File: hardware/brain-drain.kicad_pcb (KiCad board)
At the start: 4 copper layers, 136 x 100 mm, 301 parts, among them J10 SATA 22-pin, J11 SATA 22-pin, J12 SATA 22-pin, J13 SATA 22-pin, J21 KPJX-4S-S, J3 microSD, J40 Fan GND/5V/TACH/PWM, J41 OLED GND/VCC/SCL/SDA, J5 USB-C rpiboot, J50 M.2 M-key, J6 nRPIBOOT, J7 UART0 GND/TX/RX, M1 CM5002016, Q20 AO4407A, Q31 P-FET -30V 6A DFN3x3, Q32 P-FET -30V 6A DFN3x3, Q33 P-FET -30V 6A DFN3x3, Q34 P-FET -30V 6A DFN3x3, Q41 P-FET -30V 6A DFN3x3, Q42 P-FET -30V 6A DFN3x3, Q43 P-FET -30V 6A DFN3x3, Q44 P-FET -30V 6A DFN3x3, Q51 2N7002, Q52 2N7002, Q53 2N7002, Q54 2N7002, Q61 2N7002, Q62 2N7002, Q63 2N7002, Q64 2N7002, SW1 DIP x8, SW3 lid microswitch, U1 USB5744/2G, U10 ASM1153E, U11 ASM1153E, U12 ASM1153E, U13 ASM1153E, U2 USB5744/2G, U20 TPS56637RPAR, U21 TPS56637RPAR, U22 AP63203WU-7, U3 AP2112K-1.2, U50 TPS22965DSGR, U51 AP63203WU-7, U52 TPS22965DSGR, Y1 25MHz CL=20pF, Y10 30MHz CL=16pF, Y11 30MHz CL=16pF, Y12 30MHz CL=16pF, Y13 30MHz CL=16pF, Y2 25MHz CL=20pF

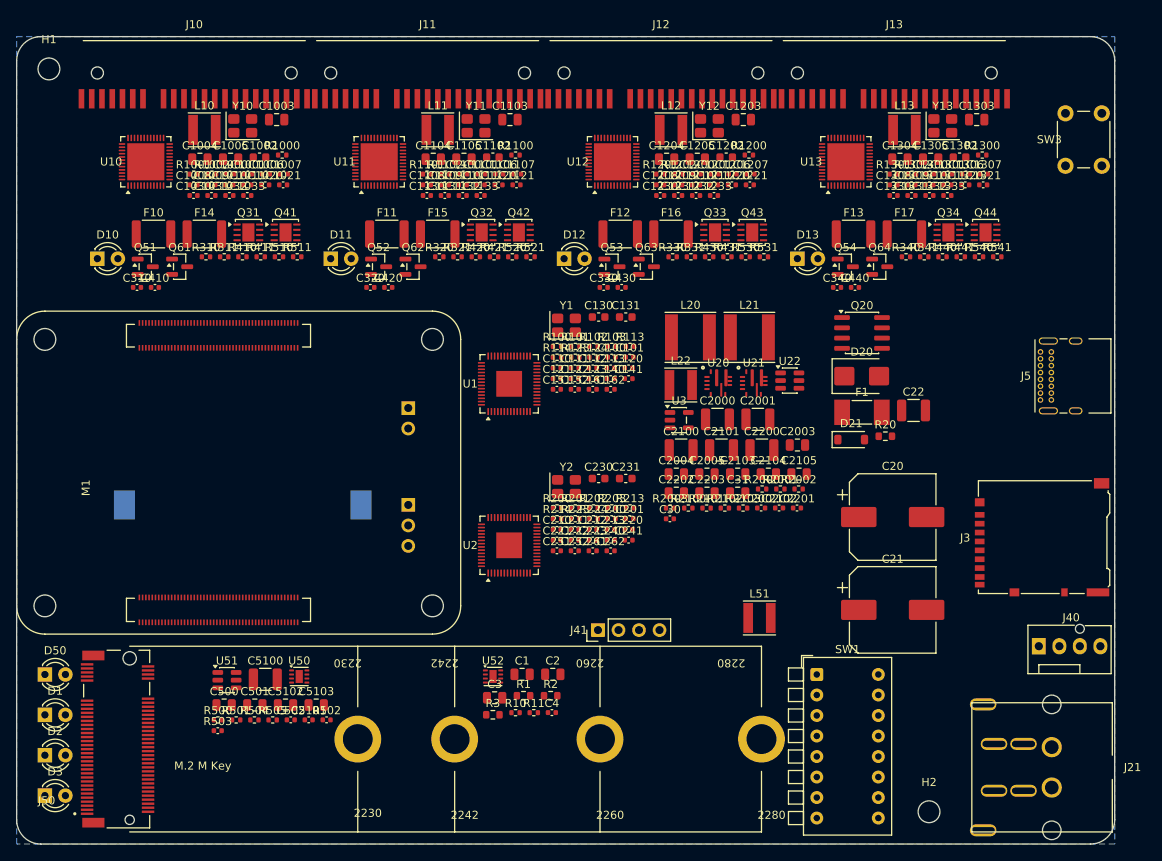
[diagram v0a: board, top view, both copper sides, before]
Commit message: hw(routing): v2 board autorouted — 75/75 signal nets, fanout and net-class fixes
- route.py: net classes written to brain-drain.kicad_pro (gen_sch.py preserves them); prepare keeps
  existing zones (deleting filled zones with fanout vias corrupts the pcbnew bindings); fanout checks
  the plane polygon instead of its bbox; import strips keep-out crossings; run_freerouting uses the
  lite DSN with -oit 2
- routed board: 930 segments / 4.4 m, 214 vias; DRC 1 known starved-thermal note, 0 clearance errors;
  499 open connections are planes, rails, bays and pairs for the hand pass
- render_board.sh: board PNGs cropped to the outline, schematic PDF + sheet PNGs
- docs: STATUS R16 closed, R4 detailed, USAGE pitfalls, CHANGELOG, tracker

Co-Authored-By: Claude Fable 5.1 <noreply@anthropic.com>
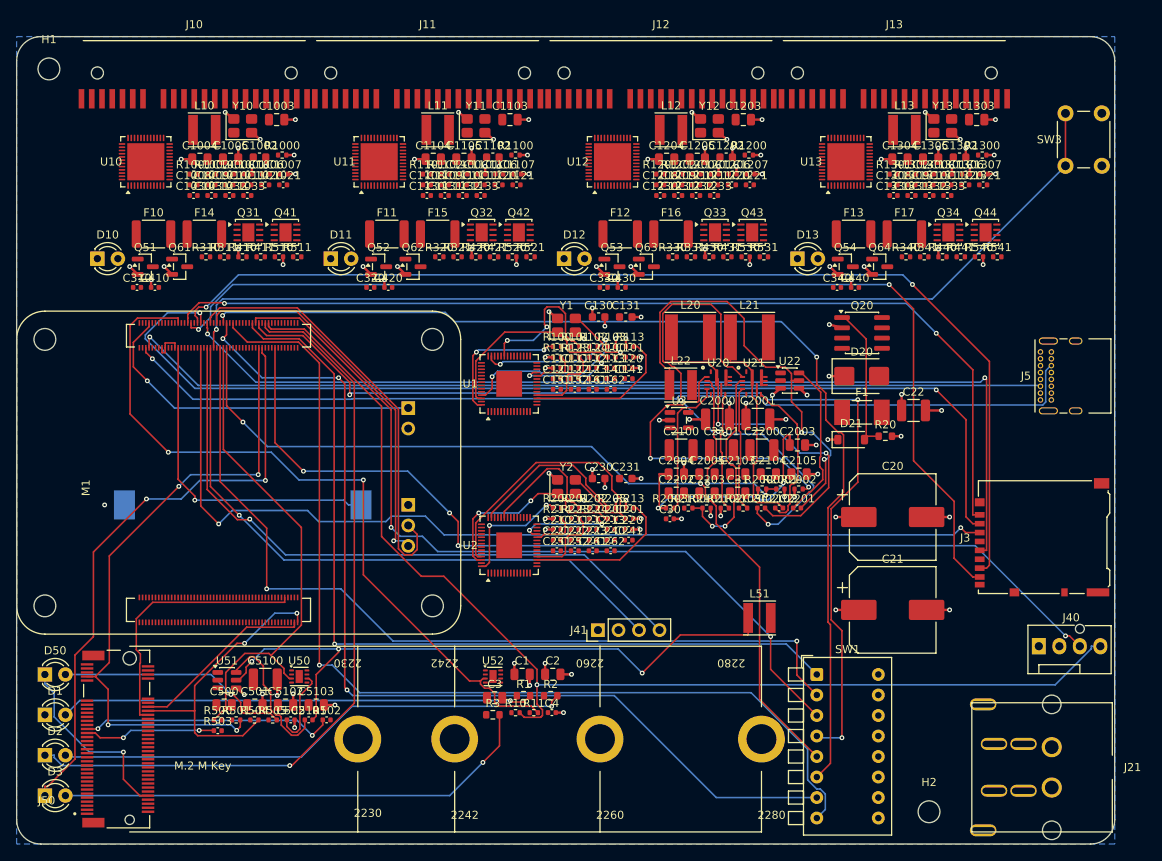
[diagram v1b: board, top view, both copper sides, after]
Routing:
- net FAN_PWM: track 0.00 -> 141.8 mm, vias 0 -> 1
- net SD_DAT0: track 0.00 -> 132.9 mm, vias 0 -> 2
- net DIP6: track 0.00 -> 132.2 mm, vias 0 -> 2
- net SD_DAT1: track 0.00 -> 131.6 mm, vias 0 -> 2
- net SD_DAT3: track 0.00 -> 129.5 mm, vias 0 -> 2
- net DIP4: track 0.00 -> 126.5 mm, vias 0 -> 3
- net DIP8: track 0.00 -> 125.4 mm, vias 0 -> 1
- net M2_DOOR: track 0.00 -> 124.2 mm, vias 0 -> 1
- net FAN_TACHO: track 0.00 -> 123.6 mm, vias 0 -> 4
- net SD_CLK: track 0.00 -> 122.7 mm, vias 0 -> 2
- net DIP7: track 0.00 -> 121.3 mm, vias 0 -> 3
- net SD_DAT2: track 0.00 -> 121.2 mm, vias 0 -> 2
- net SD_CMD: track 0.00 -> 120.1 mm, vias 0 -> 2
- net USBC_CC2: track 0.00 -> 120.1 mm, vias 0 -> 1
- net USBC_CC1: track 0.00 -> 114.2 mm, vias 0 -> 1
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
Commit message: hw(routing): CM5IO design rules, exposed-pad vias, staged router runs, fab export and open-connection report
- route.py: net classes now 0.13/0.125 mm with 0.45/0.2 vias (Power 0.5 mm, 0.6/0.3) and the
  project's minimum rules set to match; stage2/stage3 commands lock existing routes ((type fix))
  and route the remaining single-ended nets, then the pairs; fanout_big puts vias inside QFN
  exposed pads (dog-bones kept behind a flag: too many collisions at 0.4 mm pitch); pair_report
- tools/export_fab.sh: gerbers + drill zip, placement, BOM, assembly PDFs into fab/<date>/
- tools/open_report.py: open connections by group/net/part -> routing/open.md
- docs: rules in ARCHITECTURE, hardware README, FABRICATION (gates 6 and checklist), USAGE

Co-Authored-By: Claude Fable 5.1 <noreply@anthropic.com>
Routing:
- net GND: vias 85 -> 121

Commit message: hw(routing): re-placed bay rows, CM5IO rules, three-pass fanout, stage 1 routed on the new layout
- gen_pcb.py: per bay the switch block sits behind the receptacle's power pads and the bridge QFN
  behind its data pads (bay power no longer crosses the bridge); check_place clean
- route.py: fanout_conn (row-fitted vias for CM5/M.2/SATA plane pins, adjacent same-net pins bridged),
  prepare no longer re-applies classes through the API when the project has them (zone filler
  bad_alloc), Power class 0.3 mm / all clearances 0.125, stage1 command
- stage 1 imported: 1044 segments, 339 vias, 0 clearance errors; stage 2 running
- docs: STATUS R16/R21, placement text; freerouting 2.2.4/2.3.0 jars fetched for a bounded-run test
  (need Java 25, one pass took 11 min: not adopted)

Co-Authored-By: Claude Fable 5.1 <noreply@anthropic.com>
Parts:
- moved Q42 24.8 mm to (59.0, 35.4)
- moved Q44 24.8 mm to (116.8, 35.4)
- moved Q41 24.8 mm to (30.1, 35.4)
- moved Q43 24.8 mm to (87.9, 35.4)
- moved C1102 19.4 mm to (64.4, 47.6)
- moved R1100 19.4 mm to (67.2, 47.4)
- moved R1300 19.4 mm to (125.0, 47.4)
- moved C1002 19.4 mm to (35.5, 47.6)
- moved R1000 19.4 mm to (38.3, 47.4)
- moved C1202 19.4 mm to (93.3, 47.6)
- moved C1302 19.4 mm to (122.2, 47.6)
- moved R1200 19.4 mm to (96.1, 47.4)
- moved R311 19.2 mm to (28.9, 38.0)
- moved R321 19.2 mm to (57.8, 38.0)
- moved R331 19.2 mm to (86.7, 38.0)
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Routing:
- net GND: track 106.9 -> 242.4 mm, vias 121 -> 236
- net LED_nACT: track 96.3 -> 0.00 mm, vias 1 -> 0
- net 5V_SYS: track 40.5 -> 7.11 mm, vias 9 -> 3
- net U21_EN: track 45.8 -> 17.4 mm, vias 2 -> 0
- net U20_FB: track 23.7 -> 45.9 mm, vias 2 -> 0
- net DIP4: track 126.5 -> 106.1 mm, vias 3 -> 1
- net U22_SW: track 54.5 -> 34.4 mm
- net DIP3: track 101.4 -> 120.0 mm
- net I2C1_SDA: track 80.8 -> 97.3 mm
- net STATUS_LED: track 74.4 -> 90.8 mm, vias 2 -> 1
- net U20_EN: track 37.0 -> 23.2 mm
- net SD_DAT3: track 129.5 -> 117.1 mm, vias 2 -> 4
- net M2_PERn0: track 16.3 -> 28.6 mm, vias 2 -> 0
- net DIP6: track 132.2 -> 120.6 mm, vias 2 -> 3
- net U2_XTALO: track 39.0 -> 28.0 mm
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
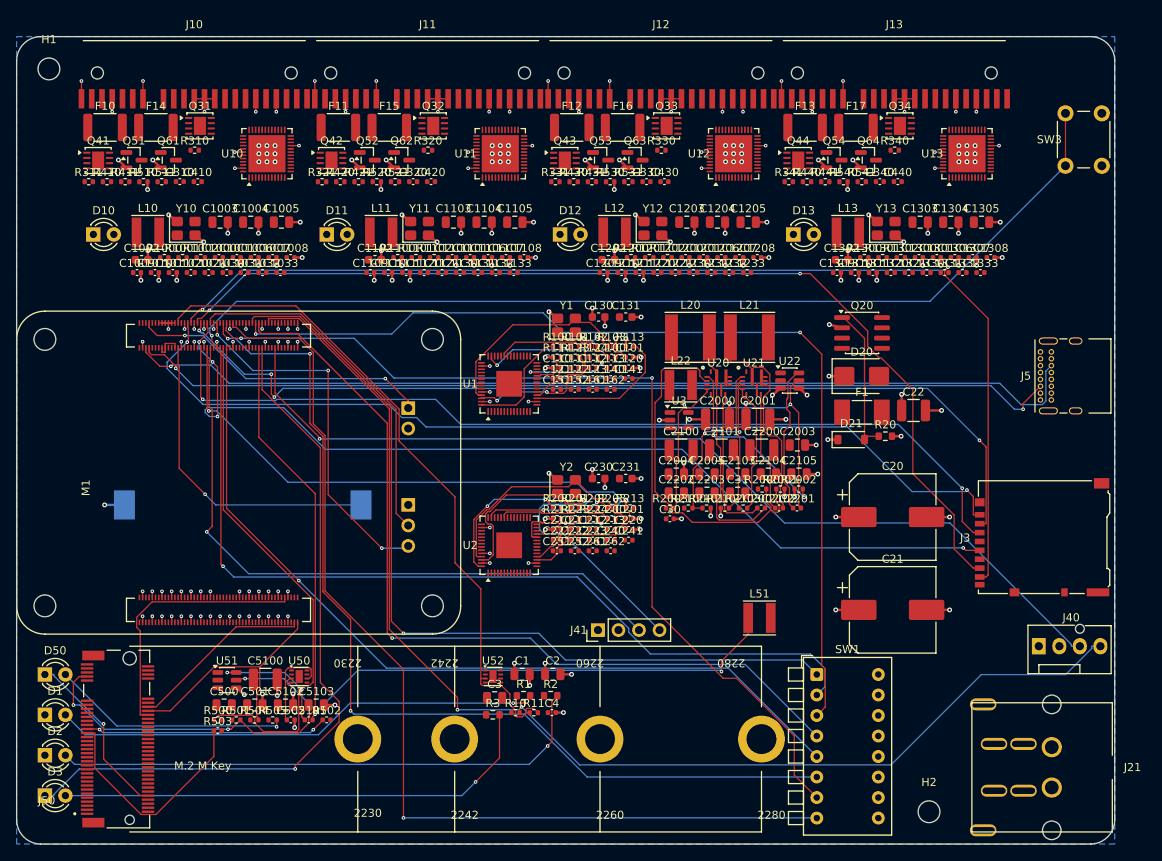
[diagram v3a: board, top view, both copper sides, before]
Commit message: hw(routing): staged autoroute complete as far as the tools go — 81 % of connections, DRC copper-clean
- board: 3175 segments (9.0 m), 658 vias; all signal nets, most plane pins; 165 connections open
  (75 plane pins in dense spots, 25 bay/rail links, 65 pair ends); 9 of 48 pairs routed, none matched
- route.py: staged runs with locked routes, -inc class ignoring (dropping nets with wiring breaks the
  DSN), BD_ROUTER/BD_PASSES for freerouting 2.4.1 on Java 25 (bounded), drc-clean, Occupancy
  geometry checks, orientation-correct pad sizes, exposed-pad ties, DRC-driven open pads, pair_report
- reports: routing/open.md, routing/pairs.md; docs: STATUS R4/R16/R21/R22, D7 (how to finish),
  USAGE staged flow, CHANGELOG, tracker, README, FABRICATION gate 1

Co-Authored-By: Claude Fable 5.1 <noreply@anthropic.com>
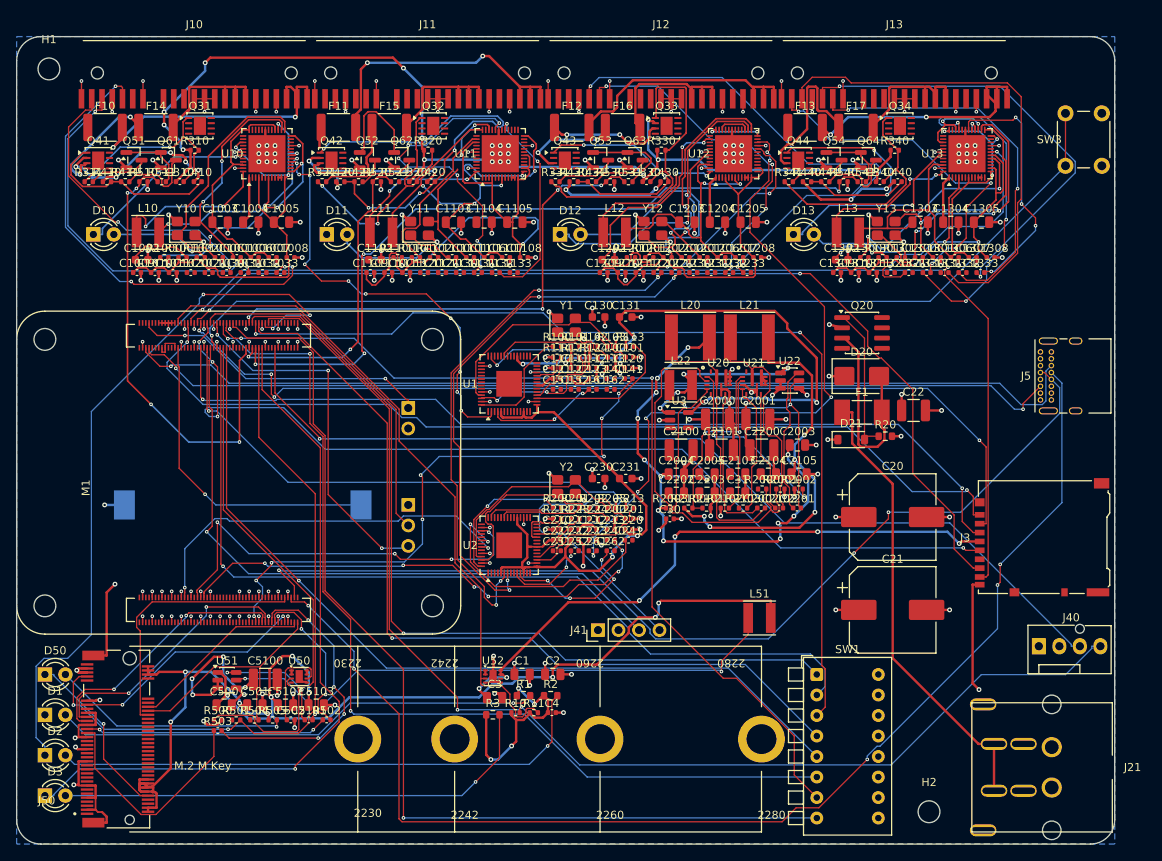
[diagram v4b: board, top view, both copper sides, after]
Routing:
- net +12V: track 17.8 -> 182.9 mm, vias 10 -> 26
- net USB2_DP: track 0.00 -> 153.9 mm, vias 0 -> 5
- net +1V2: track 0.00 -> 143.1 mm, vias 0 -> 7
- net USB2_DM: track 0.00 -> 123.0 mm, vias 0 -> 3
- net 5V_HDD: track 0.00 -> 121.3 mm, vias 0 -> 17
- net GND: track 242.4 -> 358.3 mm, vias 236 -> 250
- net 3V3_M2: track 0.00 -> 102.4 mm, vias 0 -> 7
- net BAY_EN4: track 0.00 -> 95.0 mm, vias 0 -> 4
- net 5V_SYS: track 7.11 -> 96.5 mm, vias 3 -> 16
- net LED_nACT: track 0.00 -> 88.9 mm, vias 0 -> 3
- net BAY3_USB3_RX_N: track 0.00 -> 83.3 mm, vias 0 -> 6
- net SD_VDD: track 0.00 -> 76.2 mm, vias 0 -> 6
- net U11_VCCO: track 0.00 -> 75.1 mm, vias 0 -> 4
- net USB3_0_RX_N: track 0.00 -> 72.3 mm, vias 0 -> 8
- net BAY3_USB3_TX_P: track 0.00 -> 67.0 mm, vias 0 -> 4
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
